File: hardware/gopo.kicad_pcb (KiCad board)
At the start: 4 copper layers, 99.4 x 61 mm, 143 parts, among them J3 TFT032B018, J4 SolderWire-1.5sqmm, J7 USB_C_Receptacle_USB2.0_16P, J8 2-CH UART TO ETH, Q1 BSS138P, Q2 BSS138P, Q3 SQJB60EP, Q4 BSS138P, Q5 SQJB60EP, Q6 BSS138P, Q7 IRLML6344, Q8 TSM3443CX6, SW1 BOOT / PTS810, SW2 RESET / PTS810, SW3 L-KLS4-EC1121S-E5A-F12.5, U1 AP33772SDKZ-13-FA02, U10 USBLC6-2SC6, U11 TPS55340PWPR, U12 LM74801-Q1, U13 74LVC1G08, U2 ESP32-C6-MINI-1-H4, U3 INA226, U4 BQ32000, U5 AOZ1284PI, U6 TLV431BQDBZT, Y1 32.768kHz

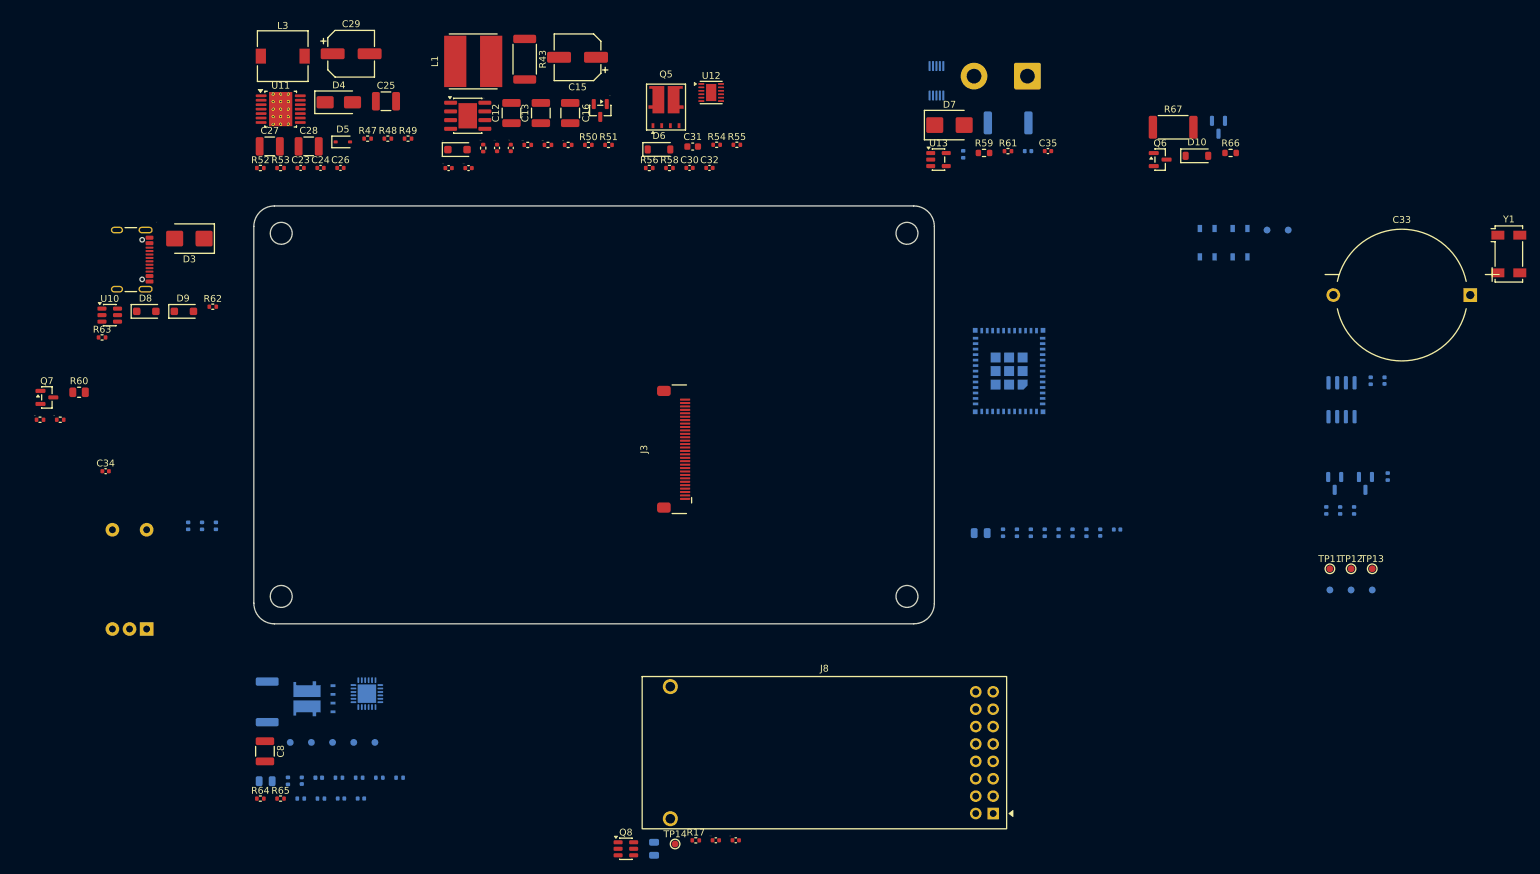
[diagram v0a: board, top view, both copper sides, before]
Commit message: PCB tasarimi guncellendi
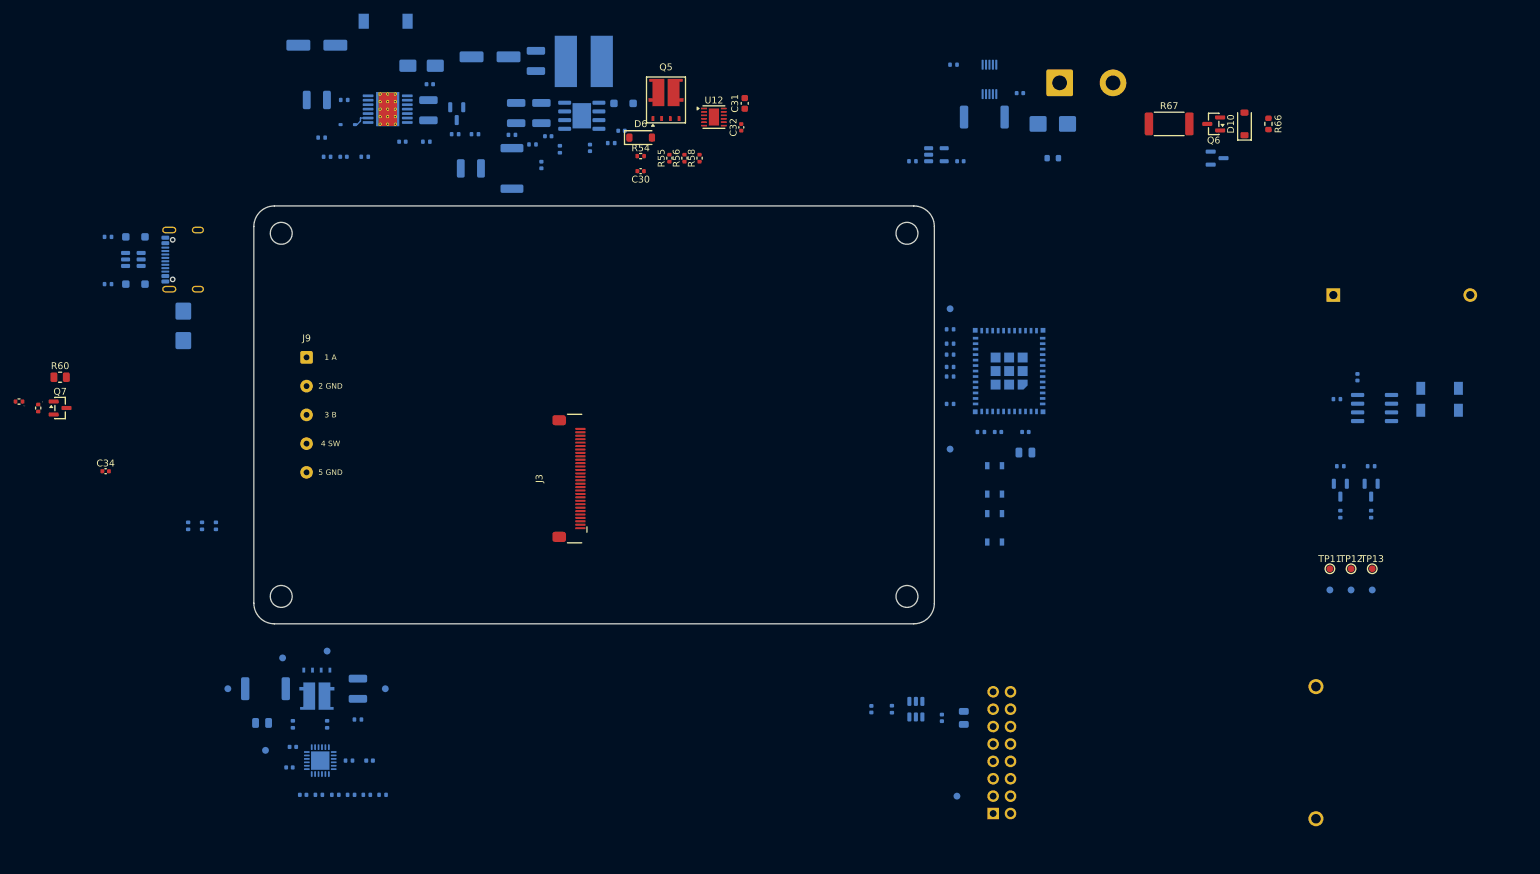
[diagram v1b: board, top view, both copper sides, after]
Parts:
- removed SW3: L-KLS4-EC1121S-E5A-F12.5, L-KLS4-EC1121S-E5A-F12.5:L-KLS4-EC1121S-E5A-F12.5
- added J9: ENCODER CABLE, Connector_Wire:SolderWire-0.25sqmm_1x05_P4.2mm_D0.65mm_OD1.7mm, F.Cu at (58.0, 91.6)
- C12, C13, C14, C15, C16, C17, C18, C19, C20, C21, C23, C24, C25, C26, C27, C28, C29, C33, C35, C8, D2, D3, D4, D5, D7, D8, D9, J7, J8, L1, L3, Q8, R17, R38, R39, R40, R41, R43, R47, R48, R49, R50, R51, R52, R53, R59, R61, R62, R63, R64, R65, TP14, U10, U11, U13, U5, U6, Y1: moved to B.Cu
- moved TP10 56.3 mm to (152.0, 105.0), turned to 0 degrees
- moved SW1 52.0 mm to (158.5, 116.5), turned to 90 degrees
- moved TP9 50.7 mm to (152.0, 84.5), turned to 0 degrees
- moved SW2 49.9 mm to (158.5, 109.5)
- moved C10 49.1 mm to (154.0, 144.3), turned to -90 degrees
- moved Q8 47.0 mm to (147.0, 143.0), turned to 90 degrees
- moved TP14 41.8 mm to (153.0, 155.7)
- moved C20 37.6 mm to (150.8, 144.3), turned to -90 degrees
- moved R17 34.5 mm to (143.5, 143.0), turned to -90 degrees
- moved R37 32.8 mm to (152.0, 91.2), turned to 0 degrees
- moved R15 32.0 mm to (152.0, 87.5), turned to 0 degrees
- moved R3 30.1 mm to (152.0, 93.0), turned to 0 degrees
- moved R10 29.3 mm to (152.0, 89.6), turned to 0 degrees
- moved R2 27.8 mm to (152.0, 94.4), turned to 0 degrees
- moved C21 27.6 mm to (140.5, 143.0), turned to -90 degrees
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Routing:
- net /USB_PD_CONTROLLER/BOOST_FB: track 0.00 -> 2.58 mm
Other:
- board text added: "1 A"
- board text added: "2 GND"
- board text added: "3 B"
- board text added: "4 SW"
- board text added: "5 GND"
- board text added: "FPC bukum yolu (R>=1.0mm, loop +1.0mm)"
- board text added: "J3 (KLS1-242I) FPC GIRISI"
- board text added: "P1"
- board text added: "P30"

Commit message: Manuel placement icin mevcut PCB durumunu kaydet
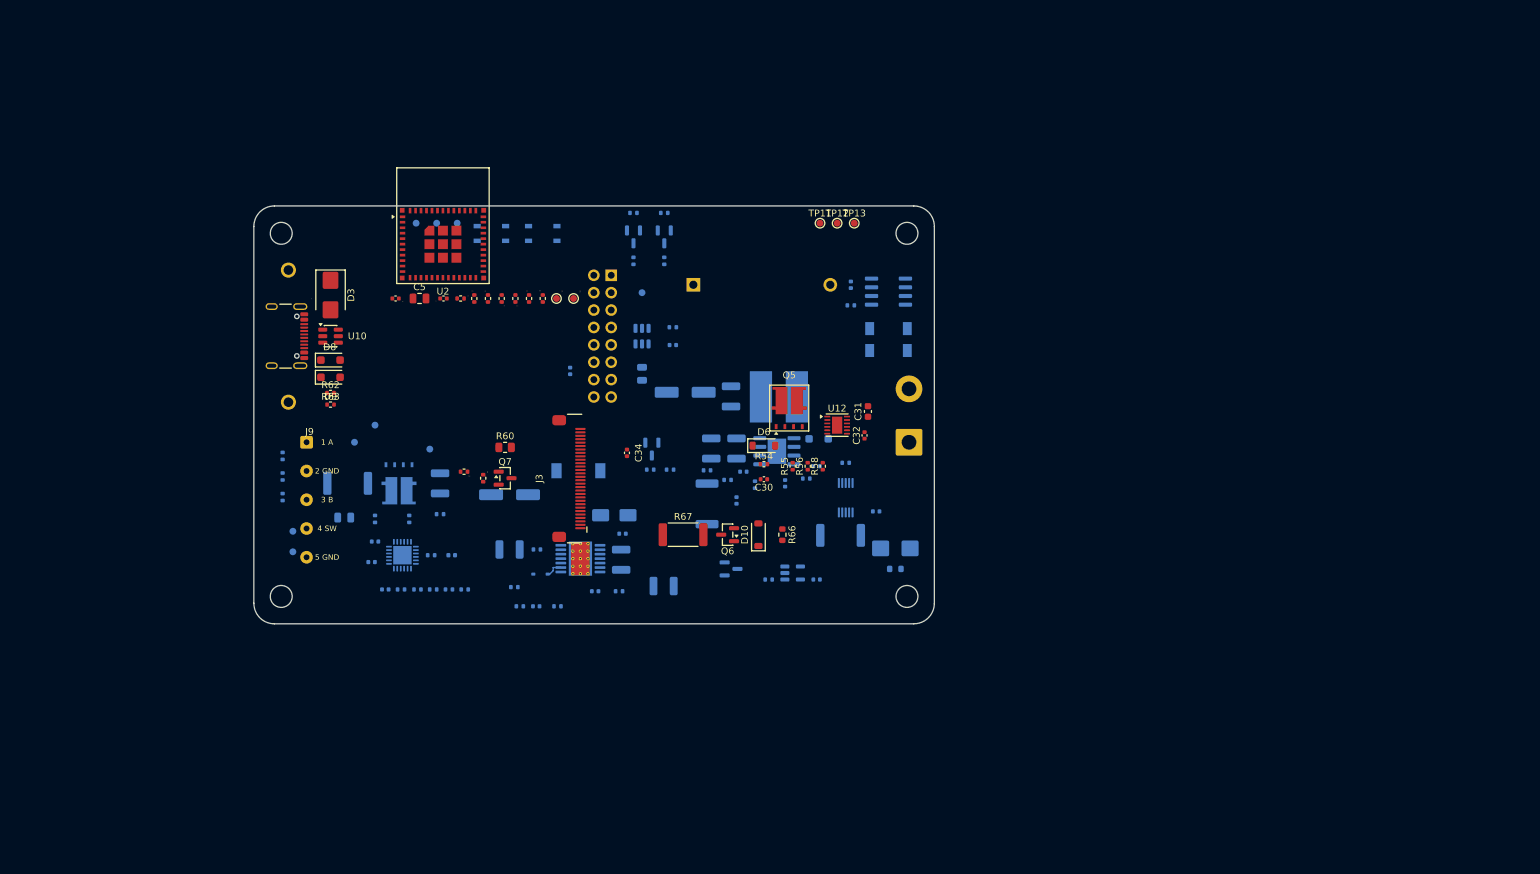
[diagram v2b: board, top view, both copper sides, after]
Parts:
- C5, C6, C7, D3, D8, D9, J7, R1, R10, R15, R16, R2, R3, R37, R62, R63, TP10, TP9, U10, U2: moved to F.Cu
- moved TP8 144.0 mm to (80.0, 72.0), turned to 0 degrees
- moved TP7 143.9 mm to (77.0, 72.0), turned to 0 degrees
- moved TP6 143.8 mm to (74.0, 72.0), turned to 0 degrees
- moved Q1 109.7 mm to (105.8, 74.0)
- moved Q2 109.7 mm to (110.2, 74.0)
- moved R4 109.7 mm to (105.8, 70.5)
- moved R5 109.7 mm to (105.8, 77.5)
- moved R6 109.7 mm to (110.2, 77.5)
- moved R7 109.7 mm to (110.2, 70.5)
- moved J8 96.4 mm to (102.5, 79.6), turned to 0 degrees
- moved C6 94.0 mm to (71.0, 83.0)
- moved C33 93.5 mm to (114.5, 81.0)
- moved D10 93.0 mm to (124.0, 117.5)
- moved Q4 93.0 mm to (120.0, 122.5)
- moved Q6 93.0 mm to (119.5, 117.5)
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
